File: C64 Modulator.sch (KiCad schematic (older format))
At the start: 36 parts, among them J1 Power, J10 , J11 , J12 , J13 , J14 , J2 8765, J3 4321, J4 AUD_STEREO, J5 TRS_3.5mm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

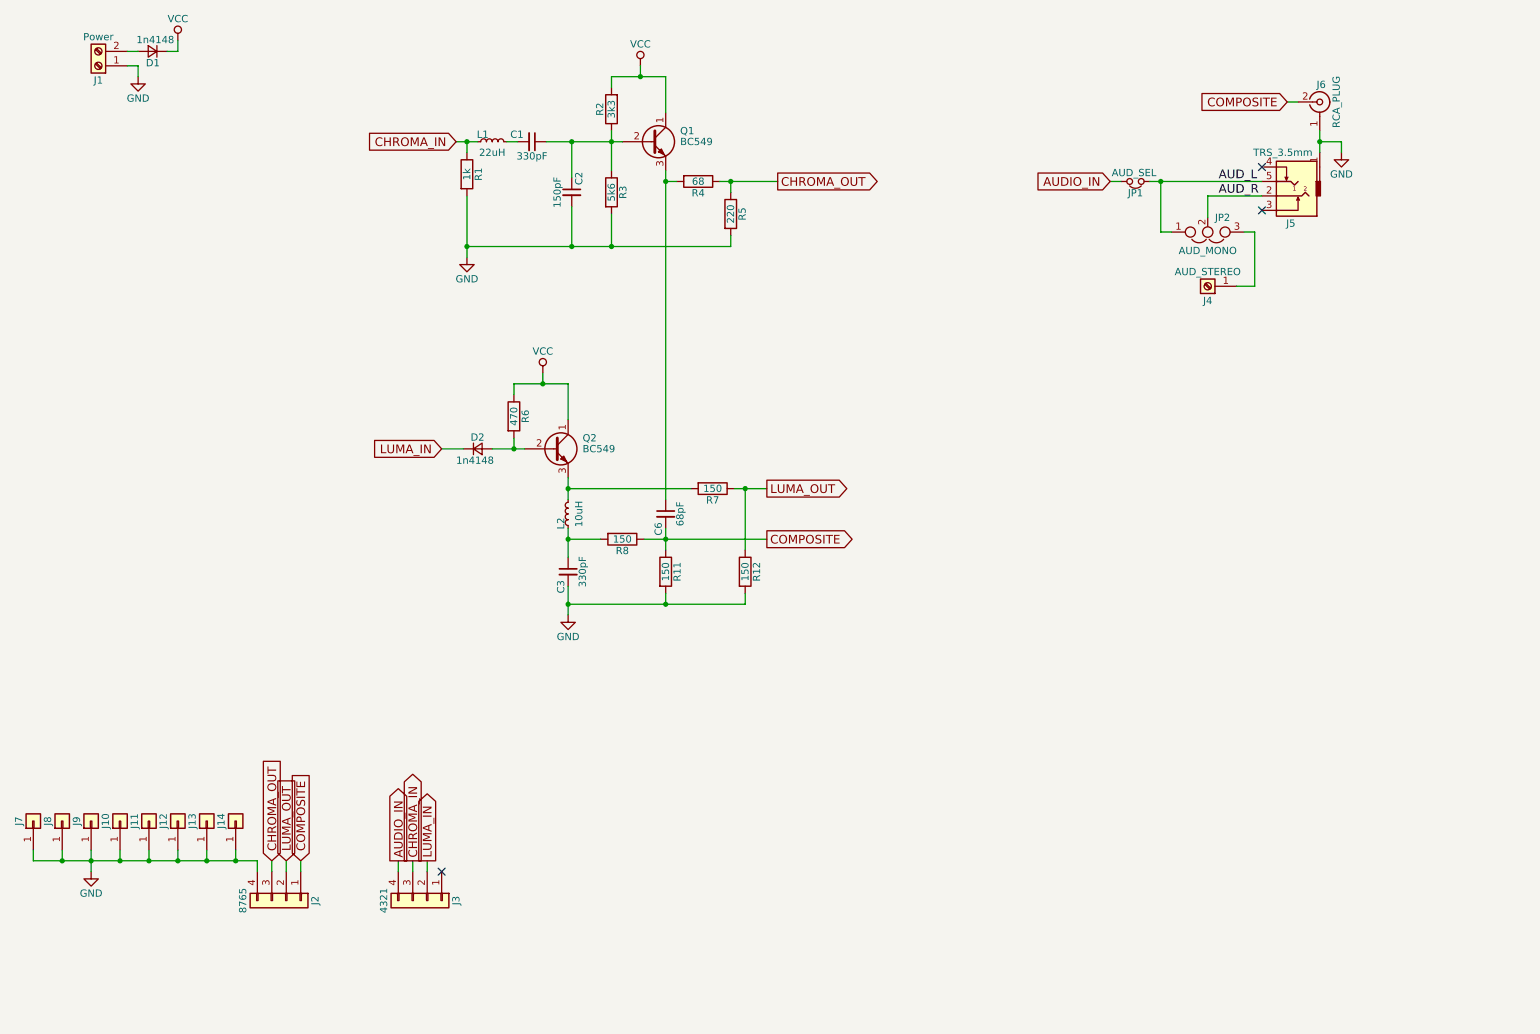
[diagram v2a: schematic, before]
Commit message: Added 5v regulator to board
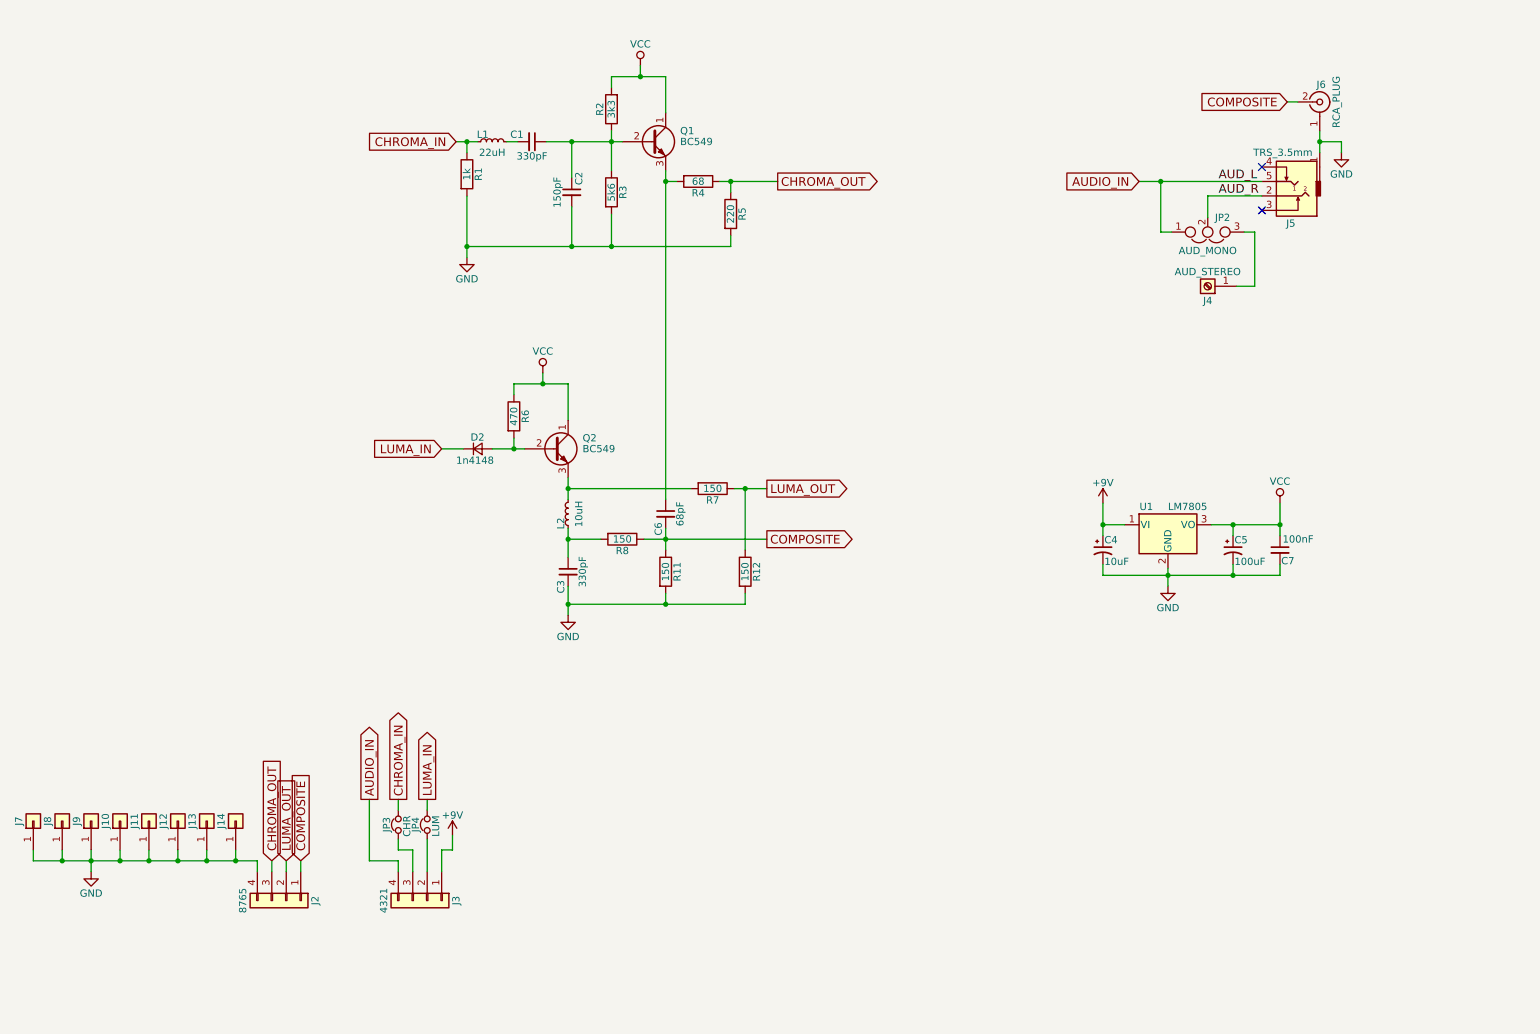
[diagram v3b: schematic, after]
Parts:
- removed D1: 1n4148, Diodes_THT:D_DO-35_SOD27_P7.62mm_Horizontal, symbol D_Small
- removed J1: Power, Pin_Headers:Pin_Header_Straight_1x02_Pitch2.54mm, symbol Screw_Terminal_01x02
- removed J2: 8765, Pin_Headers:Pin_Header_Straight_1x04_Pitch2.54mm, symbol Conn_01x04
- removed J3: 4321, Pin_Headers:Pin_Header_Straight_1x04_Pitch2.54mm, symbol Conn_01x04
- removed JP1: AUD_SEL, Pin_Headers:Pin_Header_Straight_1x02_Pitch2.54mm, symbol Jumper_NC_Small
- added C4: 10uF, Capacitors_THT:CP_Radial_D4.0mm_P2.00mm, symbol CP1_Small
- added C5: 100uF, Capacitors_THT:CP_Radial_D5.0mm_P2.50mm, symbol CP1_Small
- added C7: 100nF, Capacitors_THT:C_Disc_D4.7mm_W2.5mm_P5.00mm, symbol C_Small
- added J2: 8765, Pin_Headers:Pin_Header_Straight_1x04_Pitch2.54mm, symbol 6569_8765
- added J3: 4321, Pin_Headers:Pin_Header_Straight_1x04_Pitch2.54mm, symbol 6569_4321
- added JP3: CHR, Pin_Headers:Pin_Header_Straight_1x02_Pitch2.54mm, symbol Jumper_NC_Small
- added JP4: LUM, Pin_Headers:Pin_Header_Straight_1x02_Pitch2.54mm, symbol Jumper_NC_Small
- added U1: LM7805, TO_SOT_Packages_THT:TO-220-3_Horizontal, symbol LM7805_TO220
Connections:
- net AUD_L is gone; now on net AUDIO_IN: J5.5, JP2.1
- net AUDIO_IN: now also J3.4 (Pin_4)
- net CHROMA_IN: now also JP3.1
- net CHROMA_OUT: now also J2.3 (Pin_3)
- net COMPOSITE: now also J2.1 (Pin_1)
- net GND: now also C4.2, C5.2, C7.2, J2.4 (Pin_4), U1.2 (GND)
- net LUMA_IN: now also JP4.1
- net LUMA_OUT: now also J2.2 (Pin_2)
- net VCC: now also C5.1, C7.1, U1.3 (VO)
- new net: J3.3 (Pin_3), JP3.2
- new net: J3.2 (Pin_2), JP4.2
- new net +9V: C4.1, J3.1 (Pin_1), U1.1 (VI)
- no-connect marks 3 -> 2
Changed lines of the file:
@@
 LIBS:rca_plug
 LIBS:trs_3.5mm
+LIBS:6569_modulator
 LIBS:C64 Modulator-cache
 EELAYER 25 0
@@
 	-1   0    0    1
 $EndComp
-$Comp
-L D_Small D1
-U 1 1 5D0CF355
-P 2400 950
-F 0 "D1" H 2350 1030 50  0000 L CNN
-F 1 "1n4148" H 2250 870 50  0000 L CNN
-F 2 "Diodes_THT:D_DO-35_SOD27_P7.62mm_Horizontal" V 2400 950 50  0001 C CNN
-F 3 "" V 2400 950 50  0001 C CNN
-	1    2400 950
-	-1   0    0    1
-$EndComp
 Wire Wire Line
 	5275 4250 5275 4450
@@
 Wire Wire Line
 	5275 4650 5275 4850
-$Comp
-L Screw_Terminal_01x02 J1
-U 1 1 5D0D084B
-P 2025 1050
-F 0 "J1" H 2025 1150 50  0000 C CNN
-F 1 "Power" H 2025 850 50  0000 C CNN
-F 2 "Pin_Headers:Pin_Header_Straight_1x02_Pitch2.54mm" H 2025 1050 50  0001 C CNN
-F 3 "" H 2025 1050 50  0001 C CNN
-	1    2025 1050
-	-1   0    0    1
-$EndComp
-$Comp
-L GND #PWR03
-U 1 1 5D0D0C06
-P 2300 1125
-F 0 "#PWR03" H 2300 875 50  0001 C CNN
-F 1 "GND" H 2300 975 50  0000 C CNN
-F 2 "" H 2300 1125 50  0001 C CNN
-F 3 "" H 2300 1125 50  0001 C CNN
-	1    2300 1125
-	1    0    0    -1
-$EndComp
-Wire Wire Line
-	2225 1050 2300 1050
-Wire Wire Line
-	2300 1050 2300 1125
-Wire Wire Line
-	2225 950  2300 950
-$Comp
-L VCC #PWR04
-U 1 1 5D0D105F
-P 2575 875
-F 0 "#PWR04" H 2575 725 50  0001 C CNN
-F 1 "VCC" H 2575 1025 50  0000 C CNN
-F 2 "" H 2575 875 50  0001 C CNN
-F 3 "" H 2575 875 50  0001 C CNN
-	1    2575 875
-	1    0    0    -1
-$EndComp
-Wire Wire Line
-	2500 950  2575 950
-Wire Wire Line
-	2575 950  2575 875
 Wire Wire Line
 	5775 1050 5775 1125
@@
 Connection ~ 5100 3250
 $Comp
-L VCC #PWR05
+L VCC #PWR03
 U 1 1 5D0D18BE
 P 5100 3175
-F 0 "#PWR05" H 5100 3025 50  0001 C CNN
+F 0 "#PWR03" H 5100 3025 50  0001 C CNN
 F 1 "VCC" H 5100 3325 50  0000 C CNN
 F 2 "" H 5100 3175 50  0001 C CNN
@@
 $EndComp
 $Comp
-L GND #PWR06
+L GND #PWR04
 U 1 1 5D0D1B71
 P 5275 4850
-F 0 "#PWR06" H 5275 4600 50  0001 C CNN
+F 0 "#PWR04" H 5275 4600 50  0001 C CNN
 F 1 "GND" H 5275 4700 50  0000 C CNN
 F 2 "" H 5275 4850 50  0001 C CNN
@@
 Text GLabel 6650 4325 2    60   Output ~ 0
 COMPOSITE
-$Comp
-L Conn_01x04 J3
-U 1 1 5D0D3FDD
-P 4300 6825
-F 0 "J3" H 4300 7025 50  0000 C CNN
-F 1 "4321" H 4300 6525 50  0000 C CNN
-F 2 "Pin_Headers:Pin_Header_Straight_1x04_Pitch2.54mm" H 4300 6825 50  0001 C CNN
-F 3 "" H 4300 6825 50  0001 C CNN
-	1    4300 6825
-	0    1    1    0
-$EndComp
-Text GLabel 4300 6550 1    60   Output ~ 0
+Text GLabel 4300 6125 1    60   Output ~ 0
 LUMA_IN
 Wire Wire Line
-	4300 6625 4300 6550
-Text GLabel 4200 6550 1    60   Output ~ 0
+	4300 6400 4300 6625
+Text GLabel 4100 6125 1    60   Output ~ 0
 CHROMA_IN
 Wire Wire Line
-	4200 6625 4200 6550
-Text GLabel 4100 6550 1    60   Output ~ 0
+	4200 6475 4200 6625
+Text GLabel 3900 6125 1    60   Output ~ 0
 AUDIO_IN
-Wire Wire Line
-	4100 6625 4100 6550
-NoConn ~ 4400 6625
-$Comp
-L Conn_01x04 J2
-U 1 1 5D0D51BC
-P 3325 6825
-F 0 "J2" H 3325 7025 50  0000 C CNN
-F 1 "8765" H 3325 6525 50  0000 C CNN
-F 2 "Pin_Headers:Pin_Header_Straight_1x04_Pitch2.54mm" H 3325 6825 50  0001 C CNN
-F 3 "" H 3325 6825 50  0001 C CNN
-	1    3325 6825
-	0    1    1    0
-$EndComp
 Text GLabel 3425 6550 1    60   Input ~ 0
 COMPOSITE
@@
 	10325 1300 10250 1300
 $Comp
-L GND #PWR07
+L GND #PWR05
 U 1 1 5D0D8DCE
 P 10625 1650
-F 0 "#PWR07" H 10625 1400 50  0001 C CNN
+F 0 "#PWR05" H 10625 1400 50  0001 C CNN
 F 1 "GND" H 10625 1500 50  0000 C CNN
 F 2 "" H 10625 1650 50  0001 C CNN
@@
 NoConn ~ 10075 1750
 NoConn ~ 10075 2050
-Text GLabel 9025 1850 0    60   Input ~ 0
+Text GLabel 9225 1850 0    60   Input ~ 0
 AUDIO_IN
 $Comp
@@
 AUD_R
 Wire Wire Line
-	9025 1850 9100 1850
-$Comp
-L Jumper_NC_Small JP1
-U 1 1 5D0E0BB4
-P 9200 1850
-F 0 "JP1" H 9200 1930 50  0000 C CNN
-F 1 "AUD_SEL" H 9210 1790 50  0000 C CNN
-F 2 "Pin_Headers:Pin_Header_Straight_1x02_Pitch2.54mm" H 9200 1850 50  0001 C CNN
-F 3 "" H 9200 1850 50  0001 C CNN
-	1    9200 1850
-	-1   0    0    1
-$EndComp
+	9225 1850 10075 1850
 Wire Wire Line
 	9700 1950 10075 1950
@@
 Wire Wire Line
 	9375 2200 9375 1850
-Wire Wire Line
-	9300 1850 10075 1850
 Connection ~ 9375 1850
 Wire Wire Line
@@
 	10025 2575 9900 2575
 $Comp
-L GND #PWR08
+L GND #PWR06
 U 1 1 5D0E3D58
 P 1975 6625
-F 0 "#PWR08" H 1975 6375 50  0001 C CNN
+F 0 "#PWR06" H 1975 6375 50  0001 C CNN
 F 1 "GND" H 1975 6475 50  0000 C CNN
 F 2 "" H 1975 6625 50  0001 C CNN
@@
 	1975 6475 1975 6625
 Connection ~ 1975 6550
+$Comp
+L +9V #PWR07
+U 1 1 5D4B6616
+P 4475 6375
+F 0 "#PWR07" H 4475 6225 50  0001 C CNN
+F 1 "+9V" H 4475 6515 50  0000 C CNN
+F 2 "" H 4475 6375 50  0001 C CNN
+F 3 "" H 4475 6375 50  0001 C CNN
+	1    4475 6375
+	1    0    0    -1
+$EndComp
+Wire Wire Line
+	4400 6475 4400 6625
+$Comp
+L Jumper_NC_Small JP3
+U 1 1 5D4B7820
+P 4100 6300
+F 0 "JP3" H 4100 6380 50  0000 C CNN
+F 1 "CHR" H 4110 6240 50  0000 C CNN
+F 2 "Pin_Headers:Pin_Header_Straight_1x02_Pitch2.54mm" H 4100 6300 50  0001 C CNN
+F 3 "" H 4100 6300 50  0001 C CNN
+	1    4100 6300
+	0    -1   1    0
+$EndComp
+$Comp
+L Jumper_NC_Small JP4
+U 1 1 5D4B7C46
+P 4300 6300
+F 0 "JP4" H 4300 6380 50  0000 C CNN
+F 1 "LUM" H 4310 6240 50  0000 C CNN
+F 2 "Pin_Headers:Pin_Header_Straight_1x02_Pitch2.54mm" H 4300 6300 50  0001 C CNN
+F 3 "" H 4300 6300 50  0001 C CNN
+	1    4300 6300
+	0    -1   1    0
+$EndComp
+Wire Wire Line
+	4100 6400 4100 6475
+Wire Wire Line
+	4100 6475 4200 6475
+Wire Wire Line
+	4400 6475 4475 6475
+Wire Wire Line
+	4475 6475 4475 6375
+Wire Wire Line
+	4300 6125 4300 6200
+Wire Wire Line
+	4100 6125 4100 6200
+Wire Wire Line
+	3900 6125 3900 6550
+Wire Wire Line
+	3900 6550 4100 6550
+Wire Wire Line
+	4100 6550 4100 6625
+$Comp
+L LM7805_TO220 U1
+U 1 1 5D4BA85F
+P 9425 4225
+F 0 "U1" H 9275 4350 50  0000 C CNN
+F 1 "LM7805" H 9425 4350 50  0000 L CNN
+F 2 "TO_SOT_Packages_THT:TO-220-3_Horizontal" H 9425 4450 50  0001 C CIN
+F 3 "" H 9425 4175 50  0001 C CNN
+	1    9425 4225
+	1    0    0    -1
+$EndComp
+$Comp
+L +9V #PWR08
+U 1 1 5D4BAC44
+P 8975 4075
+F 0 "#PWR08" H 8975 3925 50  0001 C CNN
+F 1 "+9V" H 8975 4215 50  0000 C CNN
+F 2 "" H 8975 4075 50  0001 C CNN
+F 3 "" H 8975 4075 50  0001 C CNN
+	1    8975 4075
+	1    0    0    -1
+$EndComp
+$Comp
+L CP1_Small C4
+U 1 1 5D4BB37A
+P 8975 4400
+F 0 "C4" H 8985 4470 50  0000 L CNN
+F 1 "10uF" H 8985 4320 50  0000 L CNN
+F 2 "Capacitors_THT:CP_Radial_D4.0mm_P2.00mm" H 8975 4400 50  0001 C CNN
+F 3 "" H 8975 4400 50  0001 C CNN
+	1    8975 4400
+	1    0    0    -1
+$EndComp
+Wire Wire Line
+	9125 4225 8975 4225
+Wire Wire Line
+	8975 4075 8975 4300
+Connection ~ 8975 4225
+$Comp
+L CP1_Small C5
+U 1 1 5D4BBAB9
+P 9875 4400
+F 0 "C5" H 9885 4470 50  0000 L CNN
+F 1 "100uF" H 9885 4320 50  0000 L CNN
+F 2 "Capacitors_THT:CP_Radial_D5.0mm_P2.50mm" H 9875 4400 50  0001 C CNN
+F 3 "" H 9875 4400 50  0001 C CNN
+	1    9875 4400
+	1    0    0    -1
+$EndComp
+Wire Wire Line
+	9725 4225 10200 4225
+Wire Wire Line
+	9875 4300 9875 4225
+$Comp
+L C_Small C7
+U 1 1 5D4BC28F
+P 10200 4400
+F 0 "C7" H 10100 4325 50  0000 L CNN
+F 1 "100nF" H 10075 4475 50  0000 C CNN
+F 2 "Capacitors_THT:C_Disc_D4.7mm_W2.5mm_P5.00mm" H 10200 4400 50  0001 C CNN
+F 3 "" H 10200 4400 50  0001 C CNN
+	1    10200 4400
+	-1   0    0    -1
+$EndComp
+Wire Wire Line
+	10200 4075 10200 4300
+Connection ~ 9875 4225
+Wire Wire Line
+	8975 4500 8975 4575
+Wire Wire Line
+	8975 4575 10200 4575
+Wire Wire Line
+	9425 4525 9425 4650
+Wire Wire Line
+	9875 4575 9875 4500
+Connection ~ 9425 4575
+Wire Wire Line
+	10200 4575 10200 4500
+Connection ~ 9875 4575
+$Comp
+L GND #PWR09
+U 1 1 5D4BD167
+P 9425 4650
+F 0 "#PWR09" H 9425 4400 50  0001 C CNN
+F 1 "GND" H 9425 4500 50  0000 C CNN
+F 2 "" H 9425 4650 50  0001 C CNN
+F 3 "" H 9425 4650 50  0001 C CNN
+	1    9425 4650
+	1    0    0    -1
+$EndComp
+$Comp
+L VCC #PWR010
+U 1 1 5D4BD9A3
+P 10200 4075
+F 0 "#PWR010" H 10200 3925 50  0001 C CNN
+F 1 "VCC" H 10200 4225 50  0000 C CNN
+F 2 "" H 10200 4075 50  0001 C CNN
+F 3 "" H 10200 4075 50  0001 C CNN
+	1    10200 4075
+	1    0    0    -1
+$EndComp
+Connection ~ 10200 4225
+$Comp
+L 6569_4321 J3
+U 1 1 5D4BF41C
+P 4300 6825
+F 0 "J3" H 4300 7025 50  0000 C CNN
+F 1 "4321" H 4300 6525 50  0000 C CNN
+F 2 "Pin_Headers:Pin_Header_Straight_1x04_Pitch2.54mm" H 4300 6825 50  0001 C CNN
+F 3 "" H 4300 6825 50  0001 C CNN
+	1    4300 6825
+	0    1    1    0
+$EndComp
+$Comp
+L 6569_8765 J2
+U 1 1 5D4C044B
+P 3325 6825
+F 0 "J2" H 3325 7025 50  0000 C CNN
+F 1 "8765" H 3325 6525 50  0000 C CNN
+F 2 "Pin_Headers:Pin_Header_Straight_1x04_Pitch2.54mm" H 3325 6825 50  0001 C CNN
+F 3 "" H 3325 6825 50  0001 C CNN
+	1    3325 6825
+	0    1    1    0
+$EndComp
 $EndSCHEMATC

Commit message: Readded D1
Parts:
- added D1: 1n4148, Diodes_THT:D_DO-35_SOD27_P7.62mm_Horizontal, symbol D_Small
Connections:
- net VCC: now also D1.1 (K); no longer C5.1, C7.1, U1.3 (VO)
- new net: C5.1, C7.1, D1.2 (A), U1.3 (VO)
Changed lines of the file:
@@
 L VCC #PWR010
 U 1 1 5D4BD9A3
-P 10200 4075
-F 0 "#PWR010" H 10200 3925 50  0001 C CNN
-F 1 "VCC" H 10200 4225 50  0000 C CNN
-F 2 "" H 10200 4075 50  0001 C CNN
-F 3 "" H 10200 4075 50  0001 C CNN
-	1    10200 4075
+P 10200 3800
+F 0 "#PWR010" H 10200 3650 50  0001 C CNN
+F 1 "VCC" H 10200 3950 50  0000 C CNN
+F 2 "" H 10200 3800 50  0001 C CNN
+F 3 "" H 10200 3800 50  0001 C CNN
+	1    10200 3800
 	1    0    0    -1
 $EndComp
@@
 	0    1    1    0
 $EndComp
+$Comp
+L D_Small D1
+U 1 1 5D4C04C3
+P 10200 3975
+F 0 "D1" H 10150 4055 50  0000 L CNN
+F 1 "1n4148" H 10050 3895 50  0000 L CNN
+F 2 "Diodes_THT:D_DO-35_SOD27_P7.62mm_Horizontal" V 10200 3975 50  0001 C CNN
+F 3 "" V 10200 3975 50  0001 C CNN
+	1    10200 3975
+	0    1    1    0
+$EndComp
+Wire Wire Line
+	10200 3800 10200 3875
 $EndSCHEMATC
